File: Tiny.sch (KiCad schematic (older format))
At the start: 4 parts, among them IC1 MAX6126AASA25+

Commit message: committing everything
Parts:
- added C?: 0.1u, symbol Device:C
- added C?: 1u, symbol Device:C
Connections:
- net GND: now also C?.2, C?.2
- net POWER_3.3V: now also C?.1, C?.1
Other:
- moved on the sheet: C2
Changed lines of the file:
@@
 	5800 4100 5400 4100
 Wire Wire Line
-	5800 4200 5600 4200
+	5800 4200 5750 4200
 Wire Wire Line
-	5800 4300 5600 4300
+	5800 4300 5750 4300
 Wire Wire Line
-	5600 4200 5600 4300
-Connection ~ 5600 4300
-Wire Wire Line
-	5600 4300 5600 4400
+	5750 4200 5750 4300
+Connection ~ 5750 4300
 $Comp
 L power:GND #PWR0110
 U 1 1 60C94E50
-P 5400 4400
-F 0 "#PWR0110" H 5400 4150 50  0001 C CNN
-F 1 "GND" H 5405 4227 50  0000 C CNN
-F 2 "" H 5400 4400 50  0001 C CNN
-F 3 "" H 5400 4400 50  0001 C CNN
-	1    5400 4400
+P 4850 4400
+F 0 "#PWR0110" H 4850 4150 50  0001 C CNN
+F 1 "GND" H 4855 4227 50  0000 C CNN
+F 2 "" H 4850 4400 50  0001 C CNN
+F 3 "" H 4850 4400 50  0001 C CNN
+	1    4850 4400
 	1    0    0    -1
 $EndComp
@@
 L power:GND #PWR0111
 U 1 1 60C9528F
-P 5600 4400
-F 0 "#PWR0111" H 5600 4150 50  0001 C CNN
-F 1 "GND" H 5605 4227 50  0000 C CNN
-F 2 "" H 5600 4400 50  0001 C CNN
-F 3 "" H 5600 4400 50  0001 C CNN
-	1    5600 4400
+P 5750 4600
+F 0 "#PWR0111" H 5750 4350 50  0001 C CNN
+F 1 "GND" H 5755 4427 50  0000 C CNN
+F 2 "" H 5750 4600 50  0001 C CNN
+F 3 "" H 5750 4600 50  0001 C CNN
+	1    5750 4600
 	1    0    0    -1
 $EndComp
@@
 L Device:C C2
 U 1 1 60C96AC6
-P 5400 4250
-F 0 "C2" H 5285 4296 50  0000 R CNN
-F 1 "0.1u" H 5285 4205 50  0000 R CNN
-F 2 "" H 5438 4100 50  0001 C CNN
-F 3 "~" H 5400 4250 50  0001 C CNN
-	1    5400 4250
+P 4850 4250
+F 0 "C2" H 4735 4296 50  0000 R CNN
+F 1 "0.1u" H 4735 4205 50  0000 R CNN
+F 2 "" H 4888 4100 50  0001 C CNN
+F 3 "~" H 4850 4250 50  0001 C CNN
+	1    4850 4250
 	1    0    0    -1
 $EndComp
 Wire Wire Line
-	5400 4100 5200 4100
+	4850 4100 4650 4100
+Connection ~ 4850 4100
+Text Label 4650 4100 2    50   ~ 0
+POWER_3.3V
+Wire Wire Line
+	5400 4100 5400 4200
 Connection ~ 5400 4100
-Text Label 5200 4100 2    50   ~ 0
-POWER_3.3V
+Wire Wire Line
+	5400 4100 4850 4100
+$Comp
+L Device:C C?
+U 1 1 60D5F3BC
+P 5250 4350
+F 0 "C?" H 5100 4400 50  0000 R CNN
+F 1 "0.1u" H 5150 4300 50  0000 R CNN
+F 2 "" H 5288 4200 50  0001 C CNN
+F 3 "~" H 5250 4350 50  0001 C CNN
+	1    5250 4350
+	1    0    0    -1
+$EndComp
+$Comp
+L Device:C C?
+U 1 1 60D605F7
+P 5550 4350
+F 0 "C?" H 5450 4400 50  0000 R CNN
+F 1 "1u" H 5450 4300 50  0000 R CNN
+F 2 "" H 5588 4200 50  0001 C CNN
+F 3 "~" H 5550 4350 50  0001 C CNN
+	1    5550 4350
+	1    0    0    -1
+$EndComp
+Wire Wire Line
+	5400 4200 5250 4200
+Wire Wire Line
+	5400 4200 5550 4200
+Connection ~ 5400 4200
+Wire Wire Line
+	5250 4500 5400 4500
+Connection ~ 5400 4500
+Wire Wire Line
+	5400 4500 5550 4500
+Wire Wire Line
+	5750 4300 5750 4600
+$Comp
+L power:GND #PWR?
+U 1 1 60DBD2AA
+P 5400 4600
+F 0 "#PWR?" H 5400 4350 50  0001 C CNN
+F 1 "GND" H 5405 4427 50  0000 C CNN
+F 2 "" H 5400 4600 50  0001 C CNN
+F 3 "" H 5400 4600 50  0001 C CNN
+	1    5400 4600
+	1    0    0    -1
+$EndComp
+Wire Wire Line
+	5400 4500 5400 4600
 $EndSCHEMATC

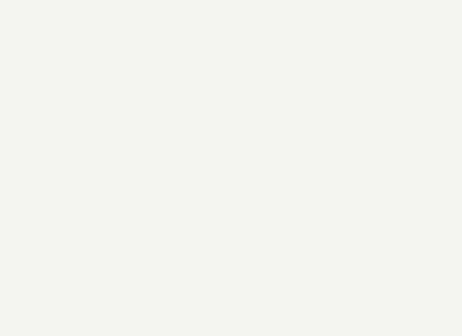
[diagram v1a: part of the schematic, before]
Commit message: reset annotations for tiny, huuge, nano; moved some refs in nano
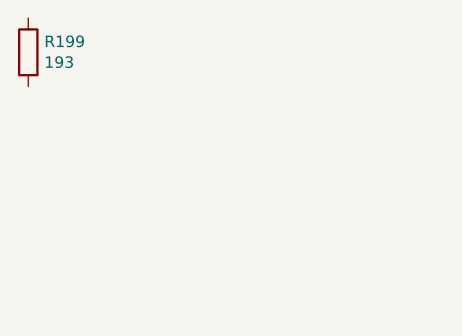
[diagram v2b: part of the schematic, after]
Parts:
- added R199: 193, symbol Device:R
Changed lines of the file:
@@
 Wire Wire Line
 	5400 4500 5400 4600
+$Comp
+L Device:R R199
+U 1 1 60CC9952
+P 3650 2300
+F 0 "R199" H 3720 2346 50  0000 L CNN
+F 1 "193" H 3720 2255 50  0000 L CNN
+F 2 "" V 3580 2300 50  0001 C CNN
+F 3 "~" H 3650 2300 50  0001 C CNN
+	1    3650 2300
+	1    0    0    -1
+$EndComp
 $EndSCHEMATC
